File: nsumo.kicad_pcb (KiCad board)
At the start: 2 copper layers, 50 x 65 mm, 74 parts, among them J1 Range_sensor_left, J10 UART, J11 Conn_01x03, J12 UNUSED, J14 MOT_FRONT_RIGHT, J15 MOT_BACK_RIGHT, J17 MOT_FRONT_LEFT, J18 MOT_BACK_LEFT, J19 Line_detector_front_left, J2 Range_sensor_front, J20 Line_detector_back_left, J21 Line_detector_front_right, J22 Line_detector_back_right, J3 BattConn1, J4 Range_sensor_front_left, J5 BattConn0, J6 I2C, J7 Range_sensor_front_right, J8 UNUSED, J9 Range_sensor_right, SW1 SW_DPST_x2, SW2 SW_SPST, U1 TSOP382xx, U2 MP2359, U3 TB6612FNG, U4 MSP430G2553IPW28, U5 AMS1117-3.3, U6 TB6612FNG, U7 AO4411

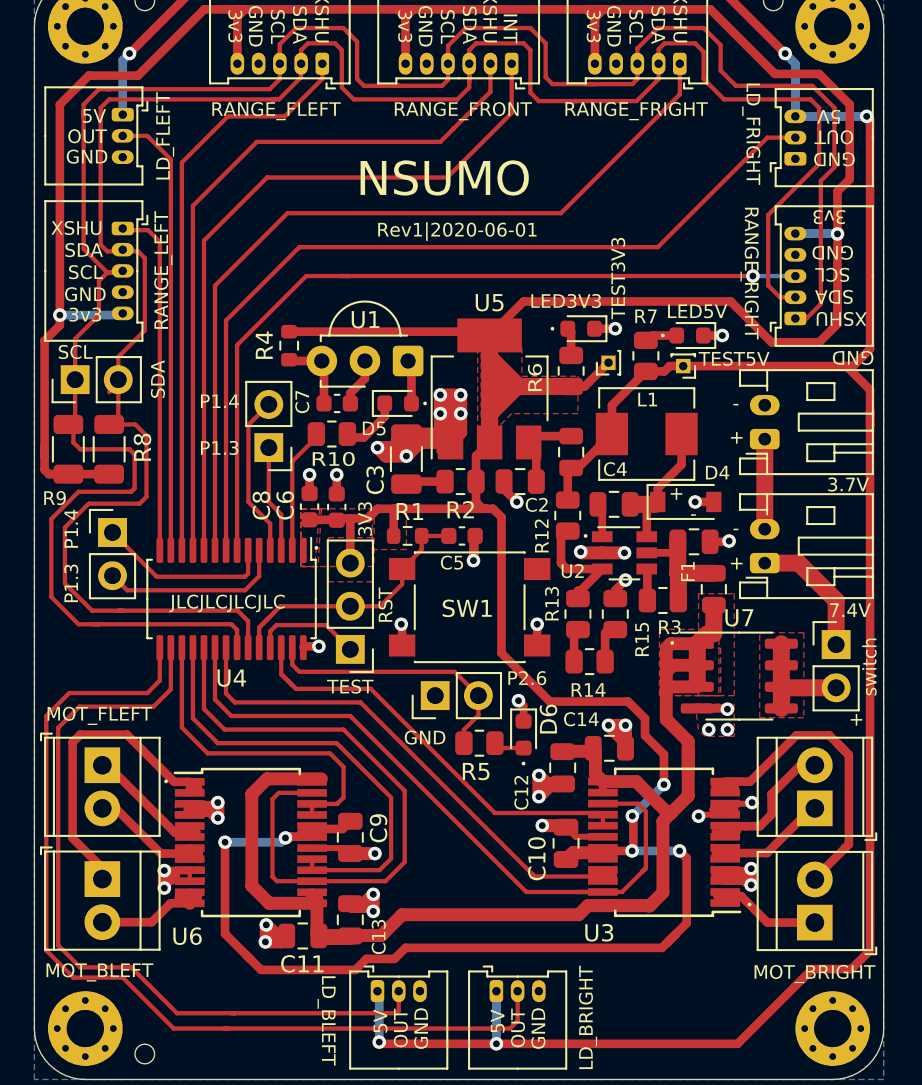
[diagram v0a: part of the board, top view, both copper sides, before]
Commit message: FIX: Change PTC fuse footprint from 0805 to 1206
There are more ones available in 1206 at Digi-Key.
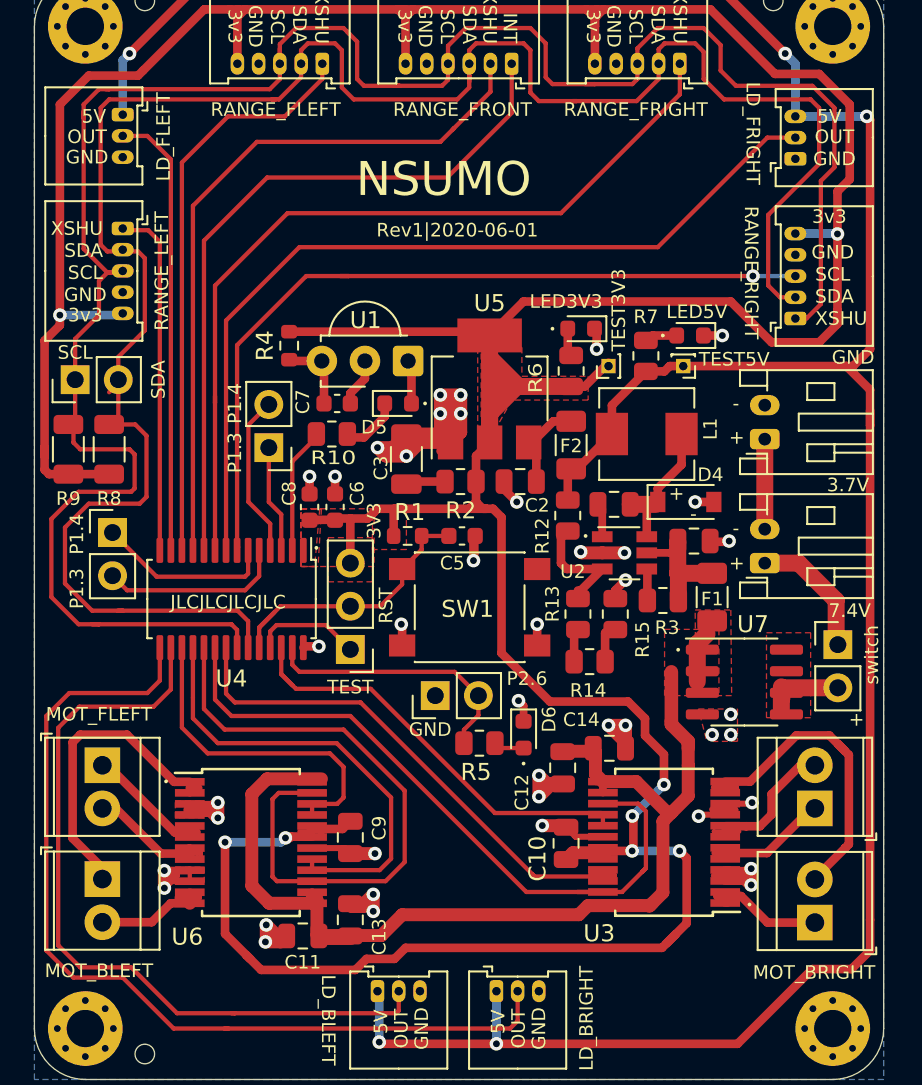
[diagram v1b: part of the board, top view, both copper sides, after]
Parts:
- F1, F2: footprint Fuse:Fuse_0805_2012Metric -> Fuse:Fuse_1206_3216Metric
- moved F1 0.47 mm to (67.9, 116.6)
- moved U7 0.46 mm to (69.8, 121.6)
- moved F2 0.41 mm to (59.6, 107.7)
- moved TP1 0.20 mm to (61.8, 103.0)
- moved C6 0.10 mm to (45.7, 111.3)
- moved SW2 0.10 mm to (75.3, 119.4)
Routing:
- net +BATT: track 86.1 -> 76.1 mm
- net Net-(SW2-Pad2): track 7.11 -> 3.88 mm
- net GND: track 114.6 -> 112.9 mm
- net Net-(C2-Pad1): track 5.14 -> 6.03 mm

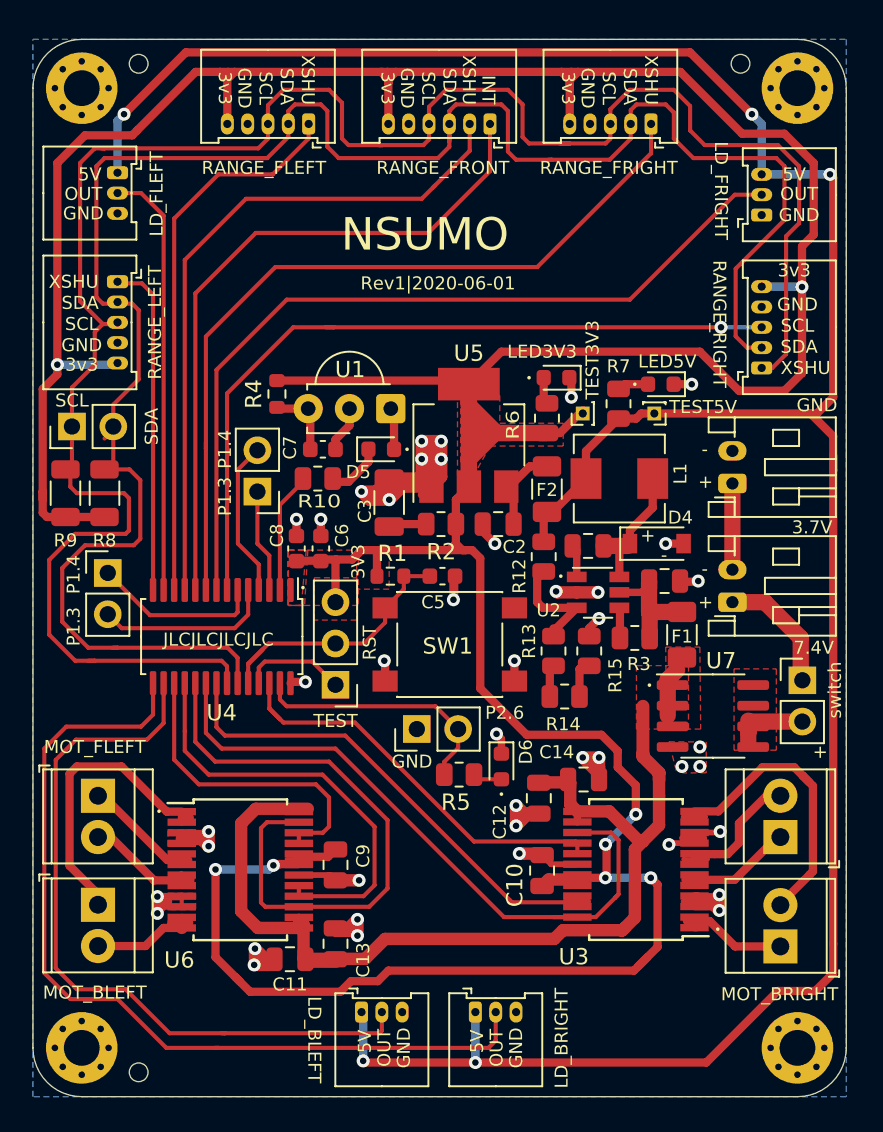
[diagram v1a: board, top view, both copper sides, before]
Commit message: ENH: REV2
First revision had several issues. Fix these for
revision 2.
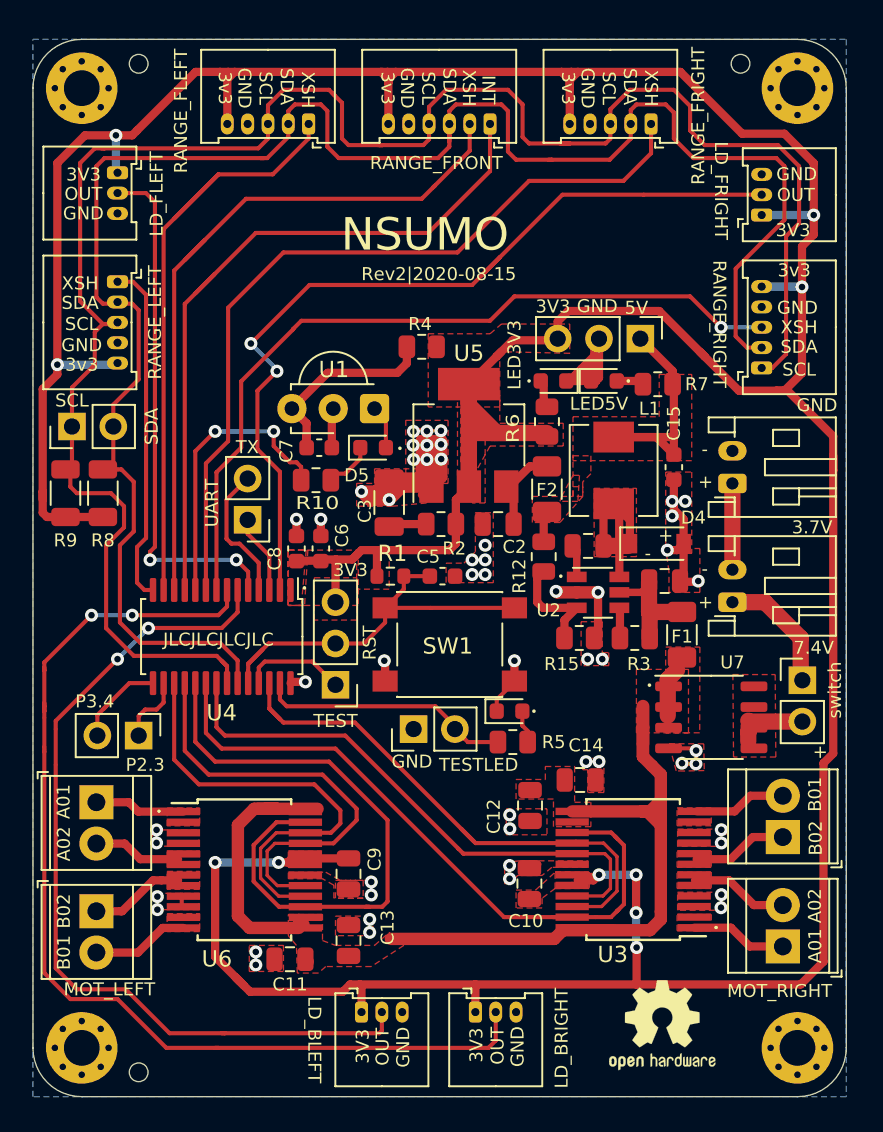
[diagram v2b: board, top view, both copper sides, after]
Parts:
- removed J18: MOT_BACK_LEFT, Custom_Connectors:TerminalBlock_TE_282834-2_1x02_P2.54mm_Horizont
- removed R13, R14: 4.7k, Resistor_SMD:R_0805_2012Metric
- removed TP1, TP2: TestPoint_Probe, Connector_PinHeader_1.00mm:PinHeader_1x01_P1.00mm_Vertical
- added C15: 22uF, Capacitor_SMD:C_0603_1608Metric, F.Cu at (67.4, 106.3)
- added J13: PWR, Connector_PinHeader_2.54mm:PinHeader_1x03_P2.54mm_Vertical, F.Cu at (65.3, 98.4)
- added J16: MOT_FRONT_LEFT, Custom_Connectors:TerminalBlock_TE_282834-2_1x02_P2.54mm_Horizont, F.Cu at (31.9, 133.6)
- added REF**: OSHW-Logo2_7.3x6mm_SilkScreen, Symbol:OSHW-Logo2_7.3x6mm_SilkScreen, F.Cu at (66.7, 140.6)
- D3: value GREEN -> YELLOW
- F1: value 1A -> 750mA
- F2: value 500mA -> 750mA
- J11: value Conn_01x03 -> SWD
- J12: value UNUSED -> LED
- J17: value MOT_FRONT_LEFT -> MOT_BACK_LEFT
- R15: value 200 -> 9.53k
- R4: footprint Resistor_SMD:R_0603_1608Metric -> Resistor_SMD:R_0805_2012Metric
- REF** (x2): footprint Custom_Connectors:DrillHoleJLC_1.152_1.3 -> Custom_Drillholes:DrillHoleJLC_1.152_1.3
- U3, U6: footprint Package_SO:SSOP-24_5.3x8.2mm_P0.65mm -> Custom_SSOP:SSOP-24_5.3x8.2mm_P0.65mm_LongPads
- U7: value AO4411 -> RS3E075AT; footprint Package_SO:SOIC-8_3.9x4.9mm_P1.27mm -> Package_SO:SOP-8_3.9x4.9mm_P1.27mm
- moved J8 10.2 mm to (34.5, 122.8), turned to 270 degrees
- moved R4 9.36 mm to (51.9, 98.9), turned to 180 degrees
- moved R5 3.86 mm to (57.5, 123.2)
- moved D3 3.51 mm to (63.1, 101.0), turned to 0 degrees
- moved D6 3.44 mm to (57.3, 121.3), turned to 0 degrees
- moved R7 2.69 mm to (66.4, 101.2), turned to 180 degrees
- moved J10 1.84 mm to (41.2, 109.5)
- moved C10 1.12 mm to (58.5, 131.9)
- moved R15 1.01 mm to (61.6, 116.8), turned to 0 degrees
- moved U1 1.00 mm to (49.0, 102.7)
- moved C9 0.97 mm to (47.4, 131.3)
- moved C13 0.82 mm to (47.4, 135.4)
- moved C12 0.70 mm to (58.6, 127.1)
- moved L1 0.61 mm to (63.7, 106.5), turned to 90 degrees
- moved D5 0.51 mm to (48.9, 105.1)
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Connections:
- net Net-(J10-Pad1) renamed UART_RX
- net Net-(J10-Pad2) renamed UART_TX
- net Net-(J15-Pad1) renamed MR_A01
- net Net-(J18-Pad2) renamed ML_B01
- net P26UNUSED renamed TEST_LED
- net xshut_front_right renamed XSHUT_FRIGHT
- net xshut_left renamed XSHUT_LEFT
- J14 pad 1: Net-(J14-Pad1) -> MR_B02
- J14 pad 2: Net-(J14-Pad2) -> MR_B01
- J15 pad 2: Net-(J15-Pad2) -> MR_A02
- J17 pad 1: Net-(J17-Pad1) -> ML_A01
- J17 pad 2: Net-(J17-Pad2) -> ML_A02
- J19 pad 1: +5V -> +3V3
- J2 pad 1: RS_FRONT_INT -> INT_FRONT
- J2 pad 2: xshut_front -> XSHUT_FRONT
- J20 pad 1: +5V -> +3V3
- J21 pad 1: GND -> +3V3
- J21 pad 3: +5V -> GND
- J22 pad 1: +5V -> +3V3
- J4 pad 1: xshut_front_left -> XSHUT_FLEFT
- J8 pad 1: P14UNUSED -> UNUSED_1
- J8 pad 2: P13UNUSED -> UNUSED_2
- J9 pad 3: xshut_right -> XSHUT_RIGHT
- R15 pad 1: Net-(R14-Pad2) -> Net-(R12-Pad2)
- R4 pad 1: Net-(C7-Pad1) -> +3V3
- R4 pad 2: +3V3 -> Net-(C7-Pad1)
- U3 pad 11: Net-(J15-Pad2) -> MR_B01
- U3 pad 12: Net-(J15-Pad2) -> MR_B01
- U3 pad 16: MOTS_RIGHT_BIN -> MOTS_RIGHT_CH2
- U3 pad 17: MOTS_RIGHT_BIN -> MOTS_RIGHT_CH1
- U3 pad 21: MOTS_RIGHT_AIN -> MOTS_RIGHT_CH1
- U3 pad 22: MOTS_RIGHT_AIN -> MOTS_RIGHT_CH2
- U3 pad 5: Net-(J14-Pad1) -> MR_A02
- U3 pad 6: Net-(J14-Pad1) -> MR_A02
- U3 pad 7: Net-(J14-Pad2) -> MR_B02
- U3 pad 8: Net-(J14-Pad2) -> MR_B02
- U4 pad 10: RS_FRONT_INT -> IR_RECEIVER
- U4 pad 11: xshut_front -> INT_FRONT
- U4 pad 12: xshut_front_left -> XSHUT_FRONT
- U4 pad 13: LD_FRONT_LEFT -> XSHUT_FLEFT
- U4 pad 15: LD_BACK_RIGHT -> UNUSED_2
- U4 pad 16: LD_BACK_LEFT -> UNUSED_1
- U4 pad 17: MOTS_LEFT_AIN -> MOTS_LEFT_CH2
- U4 pad 18: MOTS_LEFT_BIN -> MOTS_LEFT_CH1
- U4 pad 2: IR_RECEIVER -> LD_FRONT_RIGHT
- U4 pad 21: MOTS_RIGHT_AIN -> MOTS_RIGHT_CH1
- U4 pad 26: MOTS_RIGHT_BIN -> MOTS_RIGHT_CH2
- U4 pad 5: P13UNUSED -> LD_FRONT_LEFT
- U4 pad 6: P14UNUSED -> LD_BACK_LEFT
- U4 pad 7: xshut_right -> LD_BACK_RIGHT
- U4 pad 8: LD_FRONT_RIGHT -> XSHUT_RIGHT
- U6 pad 1: Net-(J18-Pad1) -> ML_A01
- U6 pad 16: MOTS_LEFT_BIN -> MOTS_LEFT_CH2
- U6 pad 17: MOTS_LEFT_BIN -> MOTS_LEFT_CH1
- U6 pad 2: Net-(J18-Pad1) -> ML_A01
- U6 pad 21: MOTS_LEFT_AIN -> MOTS_LEFT_CH1
- U6 pad 22: MOTS_LEFT_AIN -> MOTS_LEFT_CH2
- U6 pad 5: Net-(J17-Pad1) -> ML_A02
- U6 pad 6: Net-(J17-Pad1) -> ML_A02
- U6 pad 7: Net-(J17-Pad2) -> ML_B02
- U6 pad 8: Net-(J17-Pad2) -> ML_B02
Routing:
- net +5V: track 165.4 -> 18.3 mm, vias 5 -> 0
- net XSHUT_RIGHT: track 0.00 -> 48.7 mm, vias 0 -> 1
- net xshut_right: track 47.3 -> 0.00 mm, vias 1 -> 0
- net XSHUT_FRONT: track 0.00 -> 44.4 mm
- net INT_FRONT: track 0.00 -> 44.3 mm
- net xshut_front: track 42.4 -> 0.00 mm
- net RS_FRONT_INT: track 42.4 -> 0.00 mm
- net XSHUT_FLEFT: track 0.00 -> 38.4 mm
- net MOTS_RIGHT_CH1: track 0.00 -> 35.3 mm
- net xshut_front_left: track 34.3 -> 0.00 mm
- net MOTS_RIGHT_CH2: track 0.00 -> 34.1 mm
- net MOTS_RIGHT_AIN: track 32.9 -> 0.00 mm
- net GND: track 112.9 -> 80.5 mm, vias 42 -> 53
- net MOTS_LEFT_CH2: track 0.00 -> 27.6 mm
- net MOTS_LEFT_CH1: track 0.00 -> 27.3 mm
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- added copper zone on F.Cu, net +5V
- added copper zone on F.Cu, net ML_A01
- added copper zone on F.Cu, net ML_A02
- added copper zone on F.Cu, net ML_B01
- added copper zone on F.Cu, net ML_B02
- added copper zone on F.Cu, net MR_A01
- added copper zone on F.Cu, net MR_A02
- added copper zone on F.Cu, net MR_B01
- added copper zone on F.Cu, net MR_B02
- added copper zone on F.Cu, net Net-(C4-Pad2)
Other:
- board text added: "A01"
- board text added: "A02"
- board text added: "B01"
- board text added: "B02"
- board text added: "MOT_LEFT"
- board text added: "MOT_RIGHT"
- board text added: "P2.3"
- board text added: "P3.4"
- board text added: "Rev2|2020-08-15"
- board text added: "TESTLED"
- board text added: "TX"
- board text added: "UART"
- board text added: "XSH"
- board text removed: "MOT_BLEFT"
- board text removed: "MOT_BRIGHT"
- board text removed: "MOT_FLEFT"
- board text removed: "P1.3"
- board text removed: "P1.4"
- board text removed: "P2.6"
- board text removed: "Rev1|2020-06-01"
- board text removed: "TEST3V3"
- board text removed: "TEST5V"
- board text removed: "XSHU"

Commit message: FIX: Small updates to README
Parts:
- added D1: RED, LED_SMD:LED_0603_1608Metric, F.Cu at (37.9, 91.9)
- added D7: RED, LED_SMD:LED_0603_1608Metric, F.Cu at (43.8, 140.4)
- added D8: RED, LED_SMD:LED_0603_1608Metric, F.Cu at (68.3, 90.6)
- added D9: RED, LED_SMD:LED_0603_1608Metric, F.Cu at (62.0, 140.3)
- added R11: 100, Resistor_SMD:R_0805_2012Metric, F.Cu at (38.0, 90.0)
- added R13: 100, Resistor_SMD:R_0805_2012Metric, F.Cu at (41.9, 140.3)
- added R14: 100, Resistor_SMD:R_0805_2012Metric, F.Cu at (68.2, 92.5)
- added R16: 100, Resistor_SMD:R_0805_2012Metric, F.Cu at (63.8, 140.1)
- C15: footprint Capacitor_SMD:C_0603_1608Metric -> Capacitor_SMD:C_0805_2012Metric
- J19: value Line_detector_front_left -> Ld_front_left
- J20: value Line_detector_back_left -> Ld_back_left
- J21: value Line_detector_front_right -> Ld_front_right
- J22: value Line_detector_back_right -> Ld_back_right
- R10: value 0 -> 100
- R4: value 1k -> 470
- R7: value 470 -> 1k
- moved R10 10.6 mm to (51.2, 98.2), turned to -90 degrees
- moved R4 3.72 mm to (48.3, 98.0), turned to 0 degrees
- moved REF** 1.34 mm to (68.0, 140.9)
- moved C15 0.20 mm to (67.6, 106.3)
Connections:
- D5 pad 1: Net-(D5-Pad1) -> IR_RECEIVER
- R10 pad 1: Net-(D5-Pad1) -> +3V3
- R10 pad 2: IR_RECEIVER -> Net-(D5-Pad2)
- R4 pad 1: +3V3 -> Net-(C7-Pad1)
- R4 pad 2: Net-(C7-Pad1) -> +3V3
- U1 pad 1: Net-(D5-Pad2) -> IR_RECEIVER
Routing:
- net +3V3: track 295.1 -> 311.8 mm
- net LD_BACK_RIGHT: track 65.6 -> 76.8 mm
- net IR_RECEIVER: track 21.2 -> 28.1 mm
- net LD_BACK_LEFT: track 54.0 -> 60.1 mm
- net XSHUT_FLEFT: track 38.4 -> 33.5 mm
- net Net-(D5-Pad2): track 2.69 -> 6.61 mm
- net XSHUT_FRONT: track 44.4 -> 40.9 mm
- net INT_FRONT: track 44.3 -> 41.0 mm
- net Net-(C7-Pad1): track 12.6 -> 9.48 mm
- net Net-(D5-Pad1): track 2.87 -> 0.00 mm
- net Net-(D8-Pad2): track 0.00 -> 2.00 mm
- net Net-(D1-Pad2): track 0.00 -> 2.00 mm
- net Net-(D7-Pad2): track 0.00 -> 1.91 mm
- net Net-(D9-Pad2): track 0.00 -> 1.83 mm
- net LD_FRONT_LEFT: track 32.2 -> 33.8 mm
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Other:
- net class Default removed
- board text added: "Rev2|2020-08-20"
- board text removed: "Rev2|2020-08-15"

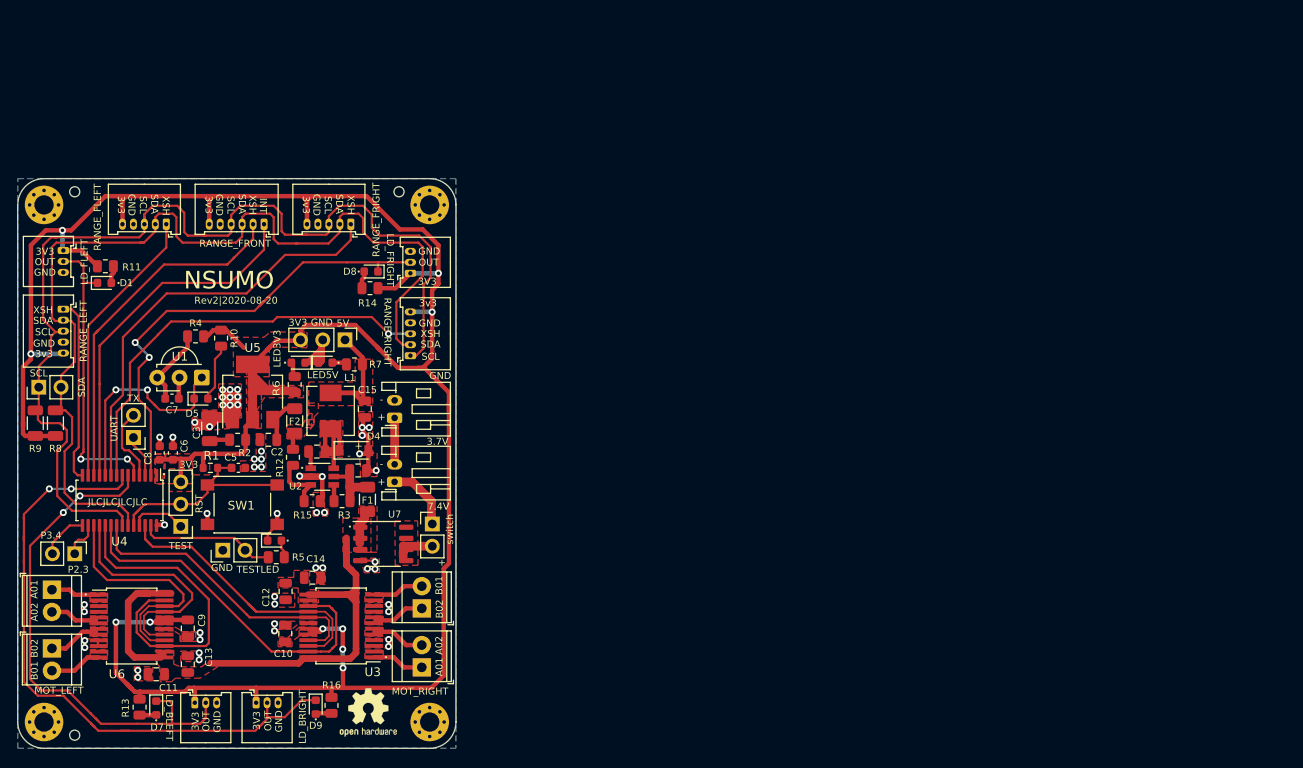
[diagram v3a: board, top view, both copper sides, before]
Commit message: ENH: Update the project for KiCad 6.0
Make the project compatible with KiCad 6.0 and add some notes
about importing it.
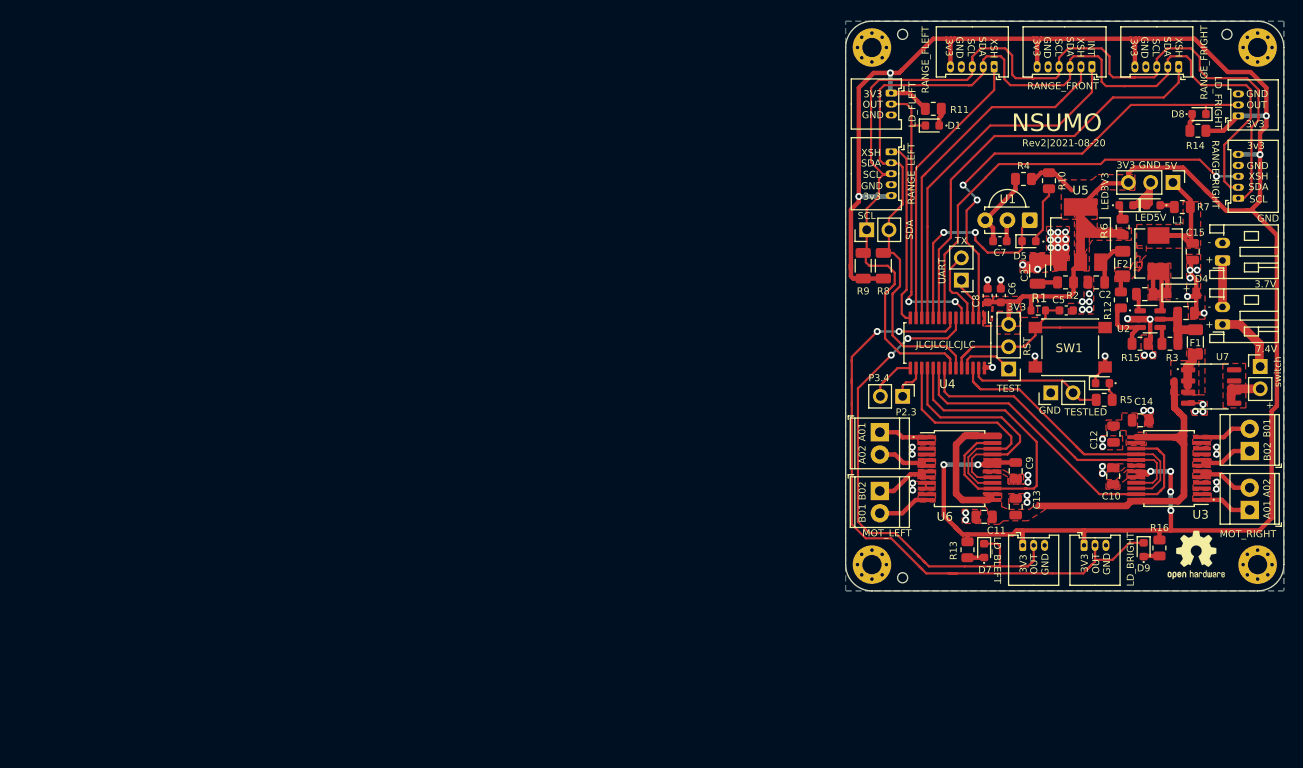
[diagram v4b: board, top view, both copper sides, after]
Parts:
- moved C12 96.2 mm to (153.0, 109.1)
- moved C13 96.2 mm to (141.9, 117.4)
- moved C15 96.2 mm to (162.1, 88.3)
- moved C2 96.2 mm to (151.1, 91.8)
- moved C3 96.2 mm to (144.4, 90.5)
- moved C7 96.2 mm to (140.1, 87.1)
- moved C9 96.2 mm to (141.9, 113.3)
- moved D2 96.2 mm to (154.5, 83.0)
- moved D3 96.2 mm to (157.6, 83.0)
- moved D4 96.2 mm to (160.8, 93.0)
- moved D5 96.2 mm to (143.4, 87.1)
- moved D8 96.2 mm to (162.8, 72.6)
- moved D9 96.2 mm to (156.5, 122.3)
- moved F1 96.2 mm to (162.4, 98.6)
- moved F2 96.2 mm to (154.1, 89.7)
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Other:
- board text added: "Rev2|2021-08-20"
- board text removed: "Rev2|2020-08-20"
